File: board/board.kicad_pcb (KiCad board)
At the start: 2 copper layers, 45 x 33 mm, 20 parts, among them J1 004_BASE-T_CT_2x3, J19 009_1000BASE-T_2x5, J20 004_BASE-T_CT_2x3, J21 009_1000BASE-T_2x5, U1 WE7490220122

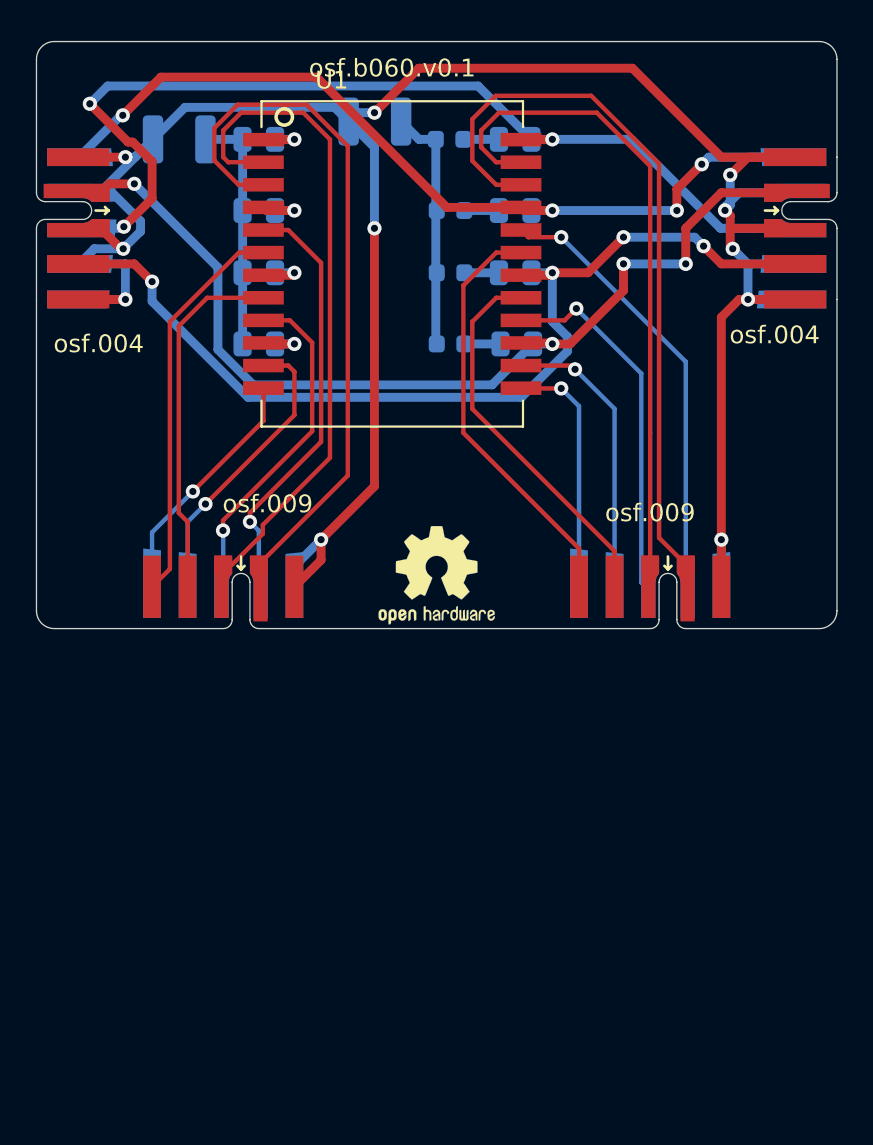
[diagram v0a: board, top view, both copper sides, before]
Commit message: refactored to use modern connectors and layout
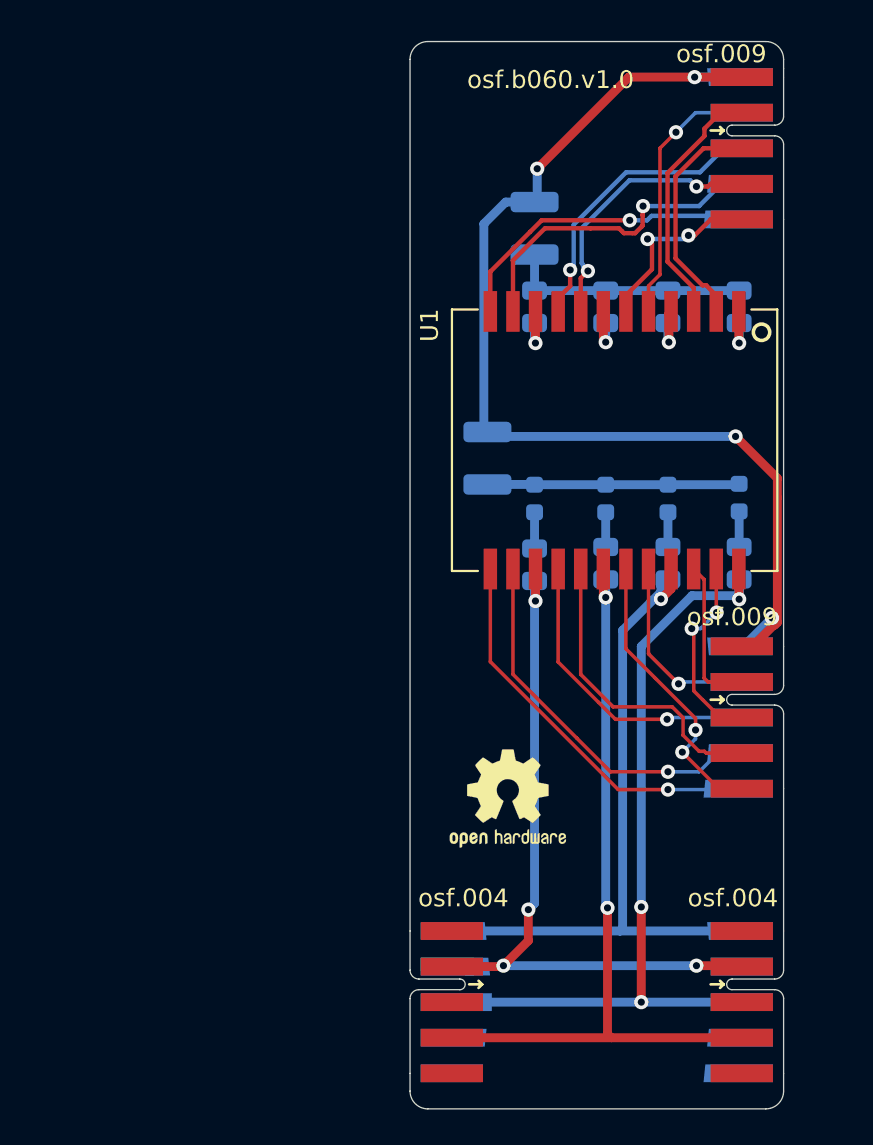
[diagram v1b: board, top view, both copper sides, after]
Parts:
- moved J1 48.3 mm to (129.5, 151.0)
- moved J20 43.6 mm to (150.5, 151.0)
- moved J21 41.5 mm to (150.5, 103.0), turned to -90 degrees
- moved R5 28.6 mm to (148.0, 111.9), turned to -90 degrees
- moved R1 26.9 mm to (148.0, 126.3), turned to 90 degrees
- moved C2 25.9 mm to (148.0, 122.6), turned to 90 degrees
- moved R6 23.6 mm to (144.0, 111.9), turned to -90 degrees
- moved R2 21.6 mm to (144.0, 126.3), turned to 90 degrees
- moved C6 20.6 mm to (136.5, 107.5), turned to -90 degrees
- moved C3 20.3 mm to (144.0, 122.7), turned to 90 degrees
- moved C1 20.0 mm to (133.8, 120.4), turned to -90 degrees
- moved R7 19.6 mm to (140.5, 111.9), turned to -90 degrees
- moved R3 17.1 mm to (140.5, 126.3), turned to 90 degrees
- moved U1 16.0 mm to (141.0, 119.4), turned to -90 degrees
- moved R8 15.6 mm to (136.5, 111.9), turned to -90 degrees
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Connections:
- J1 pad 1: Earth -> unconnected-(J1-Pad1)
- J1 pad 10: Earth -> unconnected-(J1-Pad10)
- J1 pad 3: Earth -> (no net)
- J1 pad 5: Earth -> (no net)
- J1 pad 7: Earth -> (no net)
- J1 pad 9: Earth -> unconnected-(J1-Pad9)
- J20 pad 1: Earth -> unconnected-(J20-Pad1)
- J20 pad 10: Earth -> unconnected-(J20-Pad10)
- J20 pad 3: Earth -> (no net)
- J20 pad 5: Earth -> (no net)
- J20 pad 7: Earth -> (no net)
- J20 pad 9: Earth -> unconnected-(J20-Pad9)
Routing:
- net Earth: track 149.8 -> 64.2 mm, vias 11 -> 4
- net Net-(J19-Pad2): track 41.4 -> 8.58 mm
- net Net-(J19-Pad3): track 37.1 -> 11.1 mm, vias 0 -> 2
- net Net-(J21-Pad2): track 39.8 -> 14.2 mm
- net Net-(J21-Pad3): track 37.6 -> 13.0 mm
- net Net-(J19-Pad7): track 25.2 -> 10.8 mm
- net /CT_12: track 53.7 -> 40.5 mm
- net Net-(J21-Pad5): track 22.2 -> 10.5 mm, vias 0 -> 2
- net /CT_36: track 55.2 -> 43.8 mm, vias 4 -> 2
- net /CT_78: track 57.4 -> 46.5 mm
- net Net-(J21-Pad7): track 24.3 -> 14.9 mm
- net Net-(J19-Pad10): track 13.7 -> 22.2 mm
- net /CT_45: track 48.3 -> 40.3 mm, vias 4 -> 1
- net Net-(J19-Pad5): track 23.6 -> 16.4 mm, vias 0 -> 2
- net Net-(J19-Pad9): track 16.2 -> 21.4 mm
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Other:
- board size 45 x 33 mm -> 21 x 60 mm
- board text added: "osf.b060.v1.0"
- board text removed: "osf.b060.v0.1"
